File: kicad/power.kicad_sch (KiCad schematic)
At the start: 51 parts, among them J4 TYPE-C-31-M-12, Q7 BC847BW,115, U10 MC34063AD, U11 MC34063AD, U14 XC6206P332MR-G

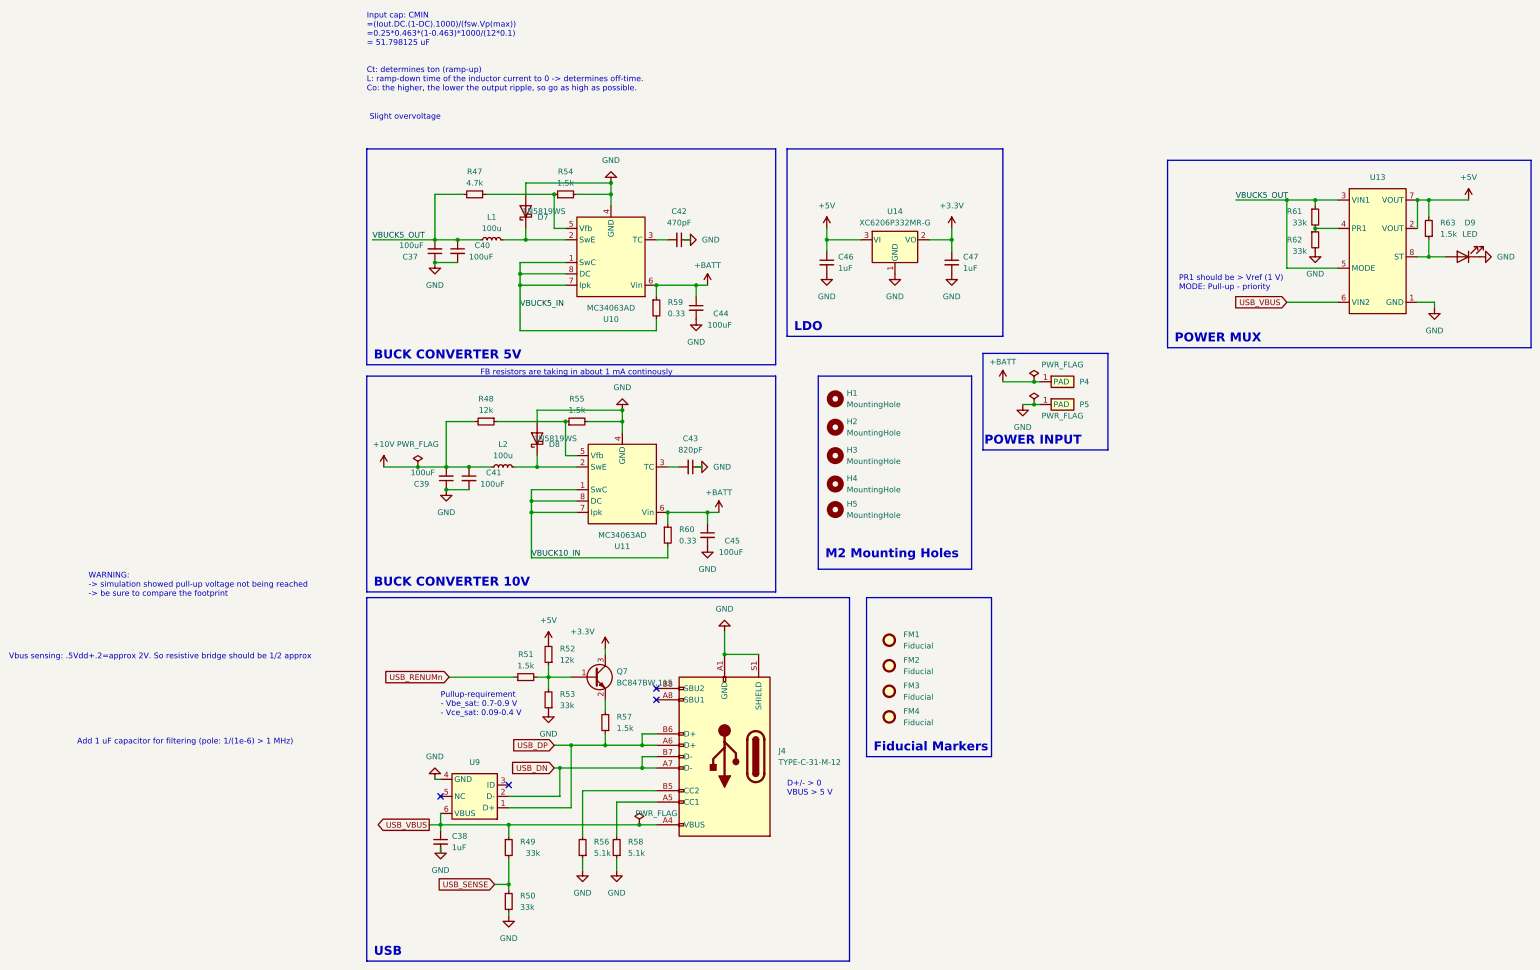
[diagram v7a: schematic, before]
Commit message: [kicad] Done first set of footprint checks, adapted connector to regular phoenix connector, found 3d models for everything but button [scripts] Checked resonator calculation [simulations] Checked bootstrap simulation [cubemx] Added extra GPIO-input + checked cpu pins
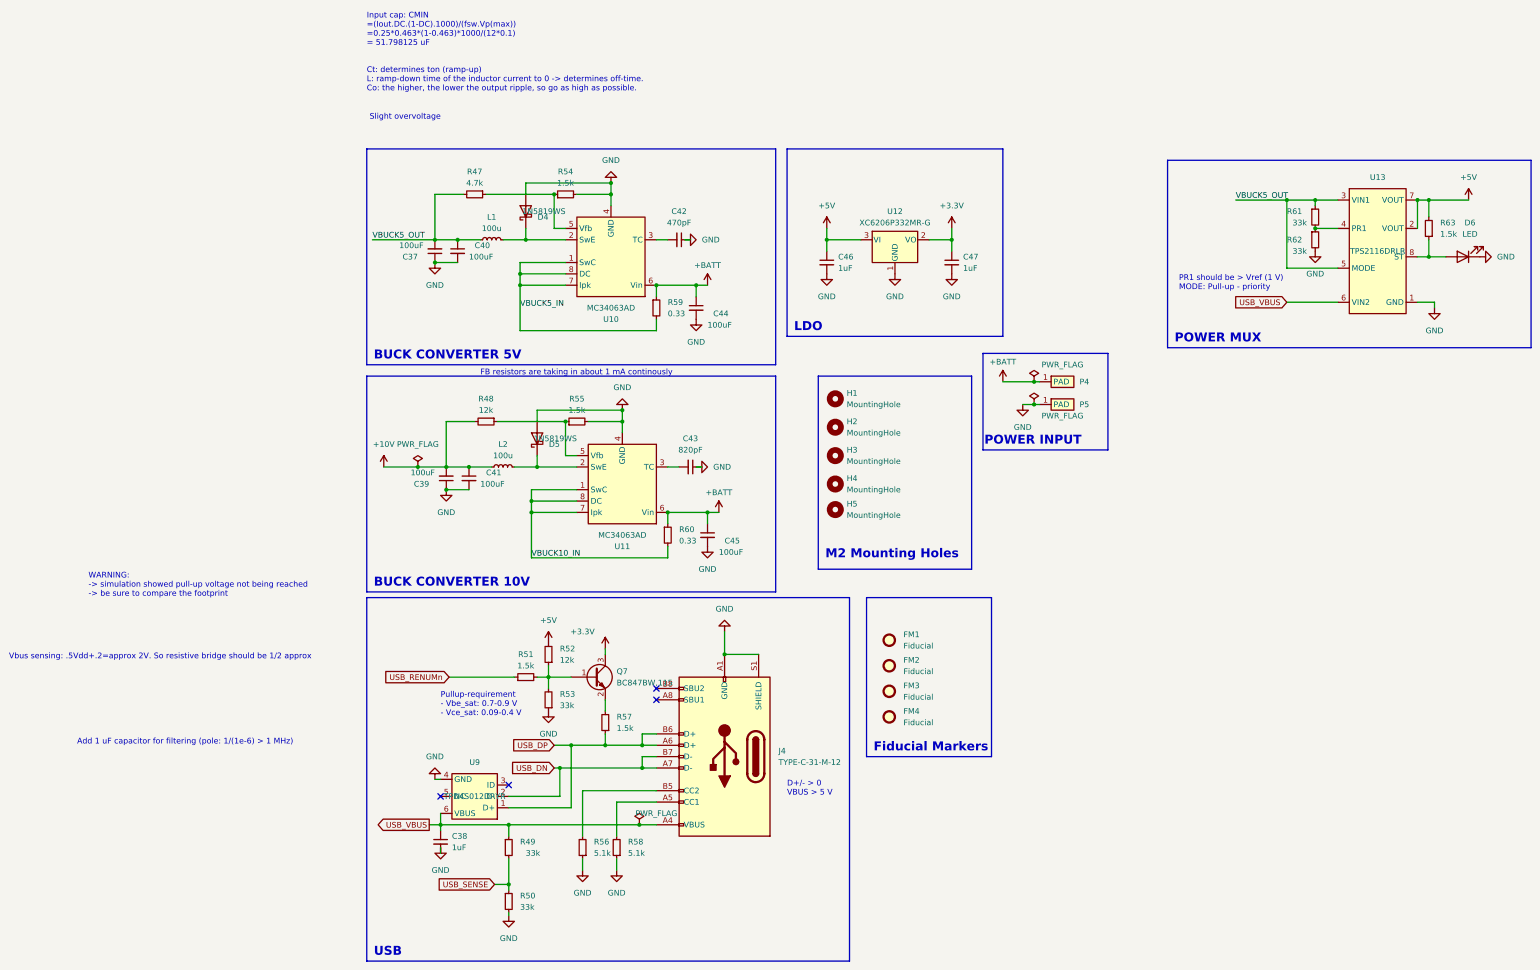
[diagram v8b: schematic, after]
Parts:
- U13: value ~ -> TPS2116DRLR
- U9: value ~ -> TPD4S012DRYR
- renumbered D7 to D4, D8 to D5, D9 to D6, U14 to U12
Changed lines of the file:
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@@
   (symbol (lib_id "Regulator_Linear:XC6206PxxxMR") (at 133.35 34.29 0) (unit 1)
     (in_bom yes) (on_board yes) (dnp no) (fields_autoplaced)
-    (property "Reference" "U14" (at 133.35 27.94 0)
+    (property "Reference" "U12" (at 133.35 27.94 0)
       (effects (font (size 1.27 1.27)))
     )
@@
       (project "bldc_project"
         (path "/91e2f46a-700b-4d7a-a06a-22469f63223f/53dc30ee-9af6-4771-8676-c78726df5d90"
-          (reference "U14") (unit 1)
+          (reference "U12") (unit 1)
         )
       )
@@
   (symbol (lib_id "Diode:1N5819") (at 53.34 78.74 90) (unit 1)
     (in_bom yes) (on_board yes) (dnp no)
-    (property "Reference" "D8" (at 58.42 80.01 90)
+    (property "Reference" "D5" (at 58.42 80.01 90)
       (effects (font (size 1.27 1.27)) (justify left))
     )
@@
       (project "bldc_project"
         (path "/91e2f46a-700b-4d7a-a06a-22469f63223f/53dc30ee-9af6-4771-8676-c78726df5d90"
-          (reference "D8") (unit 1)
+          (reference "D5") (unit 1)
         )
       )
@@
   (symbol (lib_id "Diode:1N5819") (at 50.8 27.94 90) (unit 1)
     (in_bom yes) (on_board yes) (dnp no)
-    (property "Reference" "D7" (at 55.88 29.21 90)
+    (property "Reference" "D4" (at 55.88 29.21 90)
       (effects (font (size 1.27 1.27)) (justify left))
     )
@@
       (project "bldc_project"
         (path "/91e2f46a-700b-4d7a-a06a-22469f63223f/53dc30ee-9af6-4771-8676-c78726df5d90"
-          (reference "D7") (unit 1)
+          (reference "D4") (unit 1)
         )
       )
@@
       (effects (font (size 1.27 1.27)))
     )
-    (property "Value" "~" (at 39.37 158.75 0)
+    (property "Value" "TPD4S012DRYR" (at 39.37 158.75 0)
       (effects (font (size 1.27 1.27)))
     )
@@
   (symbol (lib_id "power:PWR_FLAG") (at 164.465 71.12 0) (unit 1)
     (in_bom yes) (on_board yes) (dnp no)
-    (property "Reference" "#FLG04" (at 164.465 69.215 0)
+    (property "Reference" "#FLG05" (at 164.465 69.215 0)
       (effects (font (size 1.27 1.27)) hide)
     )
@@
       (project "bldc_project"
         (path "/91e2f46a-700b-4d7a-a06a-22469f63223f/53dc30ee-9af6-4771-8676-c78726df5d90"
-          (reference "#FLG04") (unit 1)
+          (reference "#FLG05") (unit 1)
         )
       )
@@
   (symbol (lib_id "power:PWR_FLAG") (at 76.2 165.1 0) (unit 1)
     (in_bom yes) (on_board yes) (dnp no)
-    (property "Reference" "#FLG02" (at 76.2 163.195 0)
+    (property "Reference" "#FLG03" (at 76.2 163.195 0)
       (effects (font (size 1.27 1.27)) hide)
     )
@@
       (project "bldc_project"
         (path "/91e2f46a-700b-4d7a-a06a-22469f63223f/53dc30ee-9af6-4771-8676-c78726df5d90"
-          (reference "#FLG02") (unit 1)
+          (reference "#FLG03") (unit 1)
         )
       )
@@
   (symbol (lib_id "power:PWR_FLAG") (at 26.67 85.09 0) (unit 1)
     (in_bom yes) (on_board yes) (dnp no) (fields_autoplaced)
-    (property "Reference" "#FLG01" (at 26.67 83.185 0)
+    (property "Reference" "#FLG02" (at 26.67 83.185 0)
       (effects (font (size 1.27 1.27)) hide)
     )
@@
       (project "bldc_project"
         (path "/91e2f46a-700b-4d7a-a06a-22469f63223f/53dc30ee-9af6-4771-8676-c78726df5d90"
-          (reference "#FLG01") (unit 1)
+          (reference "#FLG02") (unit 1)
         )
       )
@@
   (symbol (lib_id "Device:LED") (at 260.35 38.1 180) (unit 1)
     (in_bom yes) (on_board yes) (dnp no) (fields_autoplaced)
-    (property "Reference" "D9" (at 261.9375 30.48 0)
+    (property "Reference" "D6" (at 261.9375 30.48 0)
       (effects (font (size 1.27 1.27)))
     )
@@
       (project "bldc_project"
         (path "/91e2f46a-700b-4d7a-a06a-22469f63223f/53dc30ee-9af6-4771-8676-c78726df5d90"
-          (reference "D9") (unit 1)
+          (reference "D6") (unit 1)
         )
       )
@@
       (effects (font (size 1.27 1.27)))
     )
-    (property "Value" "~" (at 241.3 36.83 0)
+    (property "Value" "TPS2116DRLR" (at 241.3 36.83 0)
       (effects (font (size 1.27 1.27)))
     )
@@
   (symbol (lib_id "power:PWR_FLAG") (at 164.465 66.04 0) (unit 1)
     (in_bom yes) (on_board yes) (dnp no)
-    (property "Reference" "#FLG03" (at 164.465 64.135 0)
+    (property "Reference" "#FLG04" (at 164.465 64.135 0)
       (effects (font (size 1.27 1.27)) hide)
     )
@@
       (project "bldc_project"
         (path "/91e2f46a-700b-4d7a-a06a-22469f63223f/53dc30ee-9af6-4771-8676-c78726df5d90"
-          (reference "#FLG03") (unit 1)
-        )
-      )
+          (reference "#FLG04") (unit 1)
+        )
+      )
